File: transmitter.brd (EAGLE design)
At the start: 27.9 x 49.8 mm, 25 parts, among them IC1 MEGA8-AI, X1 ARK-3.5MMAPC2, X2 ARK-3.5MMAPC2, X3 ARK-3.5MMAPC2

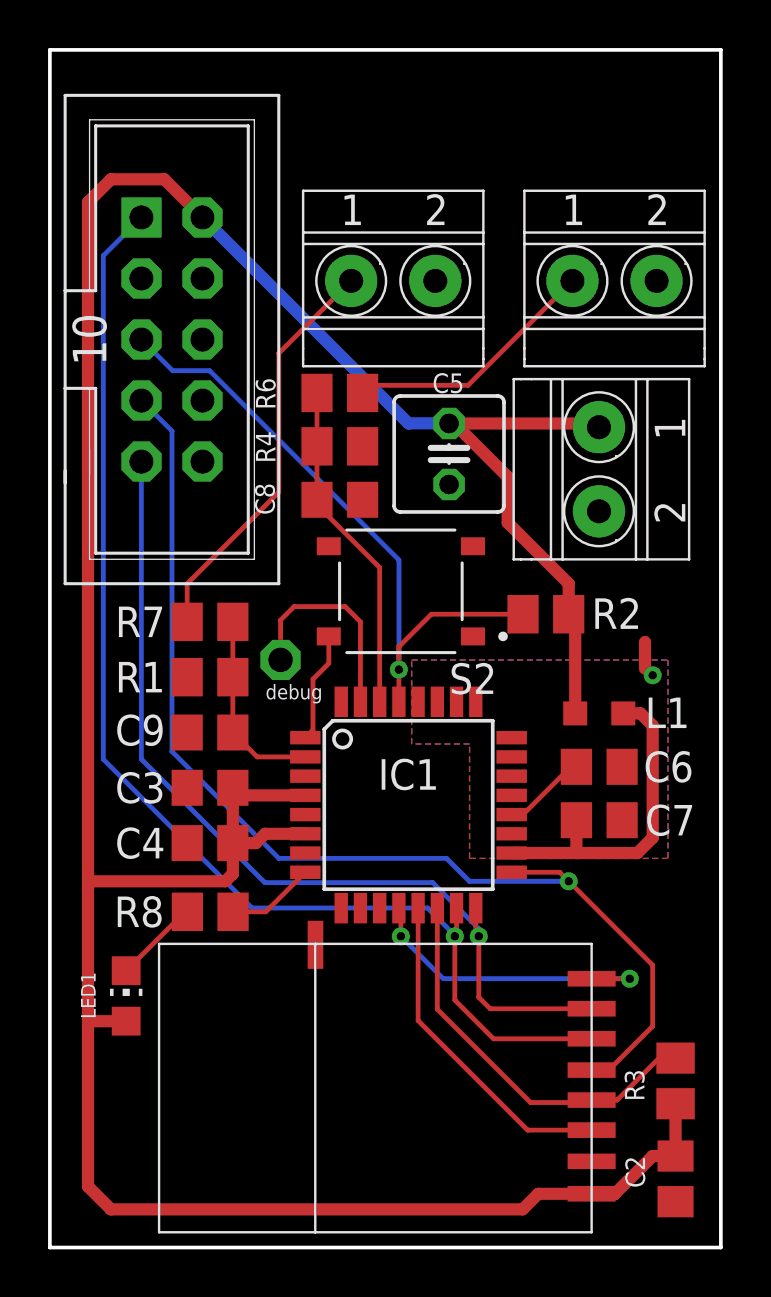
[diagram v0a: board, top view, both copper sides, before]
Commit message: usuniecie masy, przestawienie led, wiekszy opis
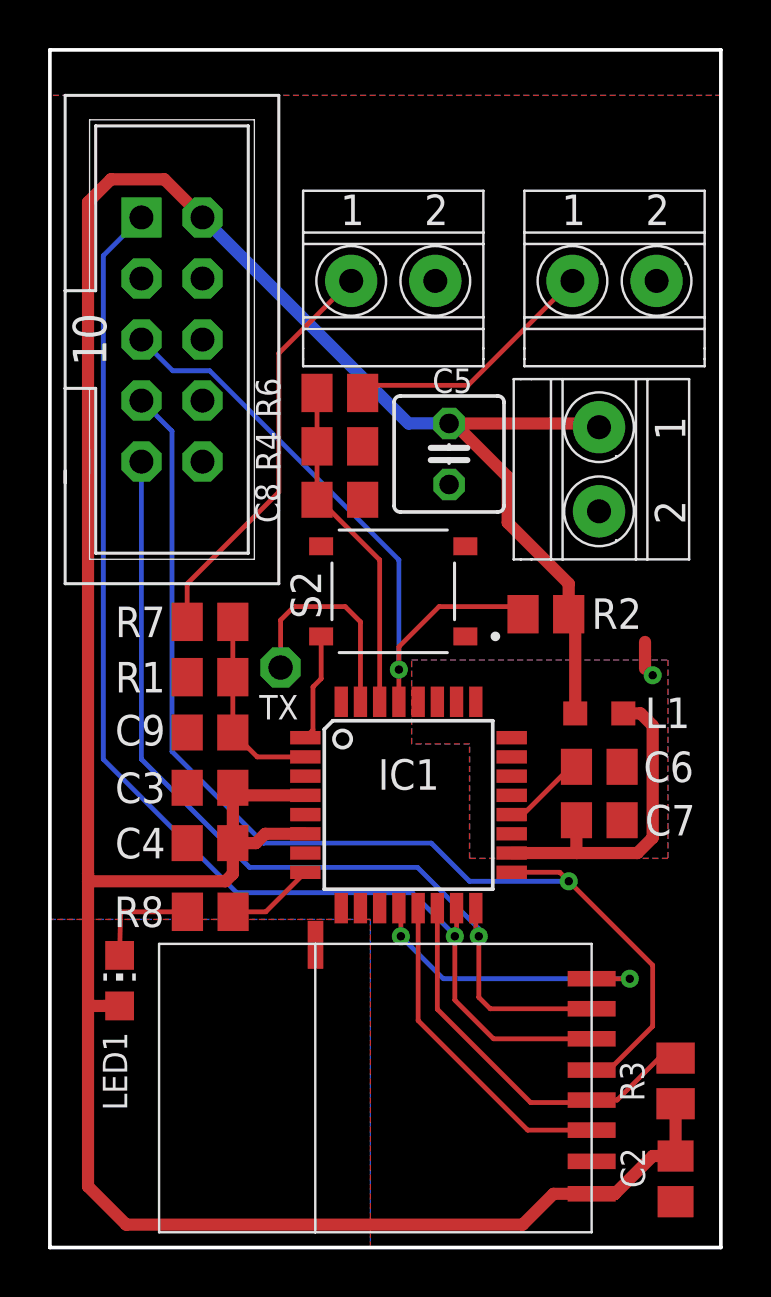
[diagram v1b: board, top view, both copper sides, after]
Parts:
- C8, C9: value 100nF -> 10nF
- R6, R7: value 1k -> 100
- moved LED1 0.69 mm to (2.90, 11.1)
- moved S2 0.32 mm to (14.3, 27.3)
- moved JP1 0.32 mm to (9.60, 24.1)
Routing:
- net N$2: track 3.56 -> 4.69 mm
- added copper zone on layer 1, net NC
- added copper zone on layer 16, net NC
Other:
- board text added: "TX"
- board text removed: "debug"

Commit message: drobne poprawki
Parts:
- removed LED1: (no value), led:CHIP-LED0805
- added LED: (no value), led:CHIP-LED0805
- added S1: REED-SWITCH-MK6-6, switch-reed:MK6-6
- moved S2 0.71 mm to (14.9, 27.0)
- moved R2 0.64 mm to (21.3, 26.4)
- moved C5 0.32 mm to (16.6, 32.7)
- moved U$1 0.06 mm to (22.6, 0.64)
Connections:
- removed net SWITCH2_WIRE: R6.2, X2.1
- new net N$3: R6.2, S1.2, X2.2
- net +3V3: now also LED.A; no longer LED1.A
- net GND: now also S1.1, X2.1; no longer X2.2
- net N$2: now also LED.C; no longer LED1.C
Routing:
- net N$3: track 0.00 -> 19.9 mm
- net SWITCH2_WIRE: track 10.7 -> 0.00 mm
- net N$2: track 4.69 -> 2.25 mm
- net RST: track 27.4 -> 28.0 mm
- net INTERRUPT_NRF: track 13.1 -> 13.6 mm
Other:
- board text added: "by Dominik Nowocien v1.1"
- board text removed: "Dominik Nowocien v1.0"
